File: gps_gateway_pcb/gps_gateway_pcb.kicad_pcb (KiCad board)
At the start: 2 copper layers, 53 x 32 mm, 72 parts, among them J1 Conn_01x06_Pin, J3 GNSS, J4 USB_OTG, J5 4G, J6 EG800, J7 SIM_Card, Q2 SS8050, Q3 SS8050, U1 Main, U2 TPS54202DDC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

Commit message: add ttl2rs485 module
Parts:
- added M1: RS485, UserLibrary:Module TTL to RS485 SMD, B.Cu at (98.3, 94.9)
- TP1: value RX -> TestPoint
- TP2: value TX -> TestPoint
- TP3: value RST -> TestPoint
- TP4: value BOOT -> TestPoint
- moved R24 1.22 mm to (93.2, 95.8)
- moved R25 1.22 mm to (93.2, 97.4)
- moved R26 1.22 mm to (93.2, 99.0)
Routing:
- net VCC33: track 77.2 -> 85.6 mm
- net /IO0: track 26.4 -> 27.5 mm
- net /IO1: track 28.5 -> 29.4 mm
- net /IO2: track 29.2 -> 28.4 mm
- net GND: vias 77 -> 80
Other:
- board text added: "BOOT"
- board text added: "RST"
- board text added: "RX"
- board text added: "TX"

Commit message: optimize pcb
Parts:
- removed D5: ST, LED_SMD:LED_0603_1608Metric
- TP1: value TestPoint -> IO5
- TP2: value TestPoint -> IO4
- TP3: value TestPoint -> RST
- TP4: value TestPoint -> BOOT
- moved TP2 11.7 mm to (88.1, 105.3)
- moved TP1 10.3 mm to (84.6, 104.4)
- moved R4 2.72 mm to (79.6, 109.0), turned to -90 degrees
- moved D4 1.91 mm to (91.5, 106.1)
- moved R9 1.12 mm to (91.5, 104.4), turned to 0 degrees
- moved R10 0.66 mm to (91.5, 102.8)
- moved R6 0.54 mm to (86.9, 106.8)
- moved R8 0.53 mm to (90.8, 100.0)
- moved R3 0.29 mm to (88.9, 106.8)
- moved R7 0.29 mm to (88.9, 103.7)
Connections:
- TP1 pad 1: /ESP_RX0 -> /IO5
- TP2 pad 1: /ESP_TX0 -> /IO4
- U3 pad 10: /ESP_TX_SIM -> /IO5
- U3 pad 27: /ESP_RX0 -> /ESP_RX_SIM
- U3 pad 28: /ESP_TX0 -> /ESP_TX_SIM
- U3 pad 9: /ESP_RX_SIM -> /IO4
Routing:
- net /ESP_TX_SIM: track 37.3 -> 28.1 mm
- net /ESP_RX_SIM: track 38.6 -> 31.7 mm
- net /IO4: track 0.00 -> 5.55 mm, vias 0 -> 1
- net /ESP_RX0: track 4.86 -> 0.00 mm, vias 1 -> 0
- net Net-(AE1-FEED): track 6.65 -> 4.13 mm
- net /IO5: track 0.00 -> 2.15 mm, vias 0 -> 1
- net GND: track 350.7 -> 348.7 mm, vias 80 -> 85
- net Net-(D6-A): track 5.18 -> 3.47 mm
- net /ESP_TX0: track 1.22 -> 0.00 mm, vias 1 -> 0
- net /Status: track 9.51 -> 8.86 mm
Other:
- board text added: "4G"
- board text added: "GPS"

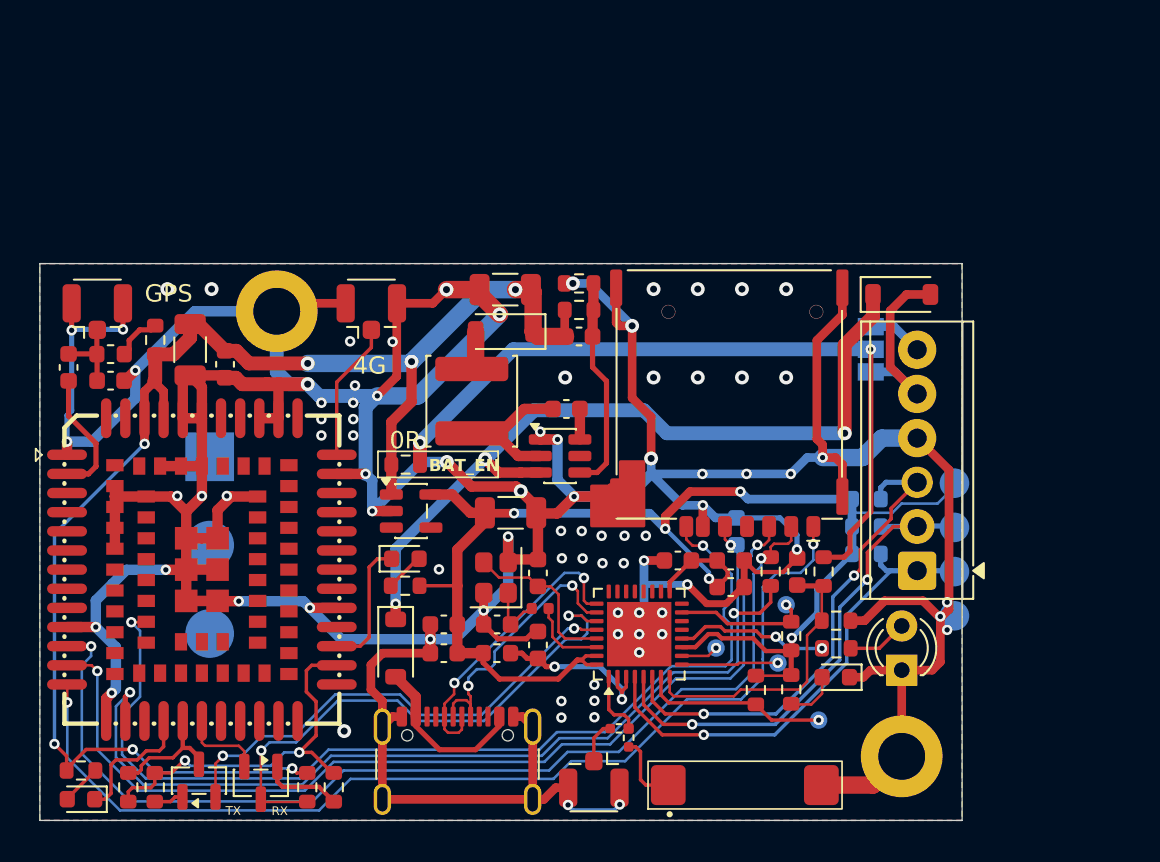
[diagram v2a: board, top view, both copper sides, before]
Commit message: change size
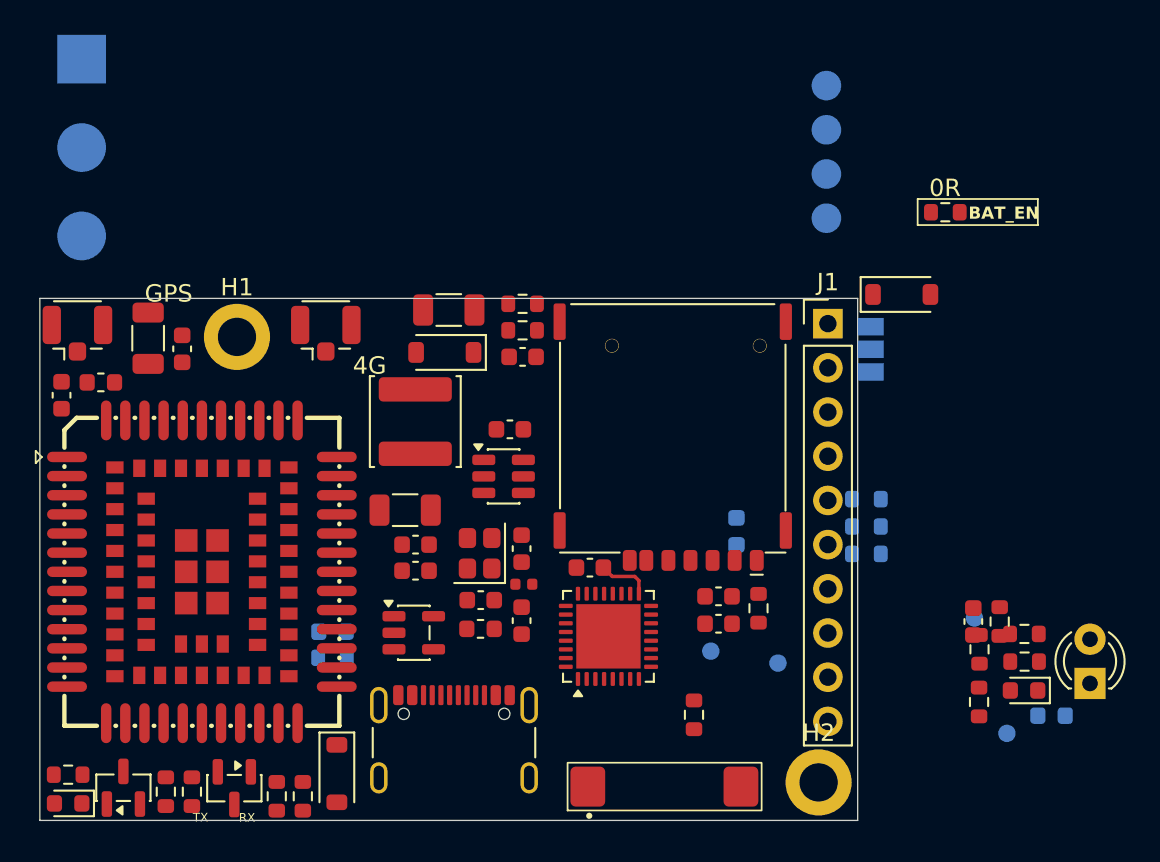
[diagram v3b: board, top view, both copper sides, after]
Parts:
- removed C19: 10uF, Capacitor_SMD:C_0603_1608Metric
- removed R11: 10, Resistor_SMD:R_0603_1608Metric
- removed R4: Res_3Pin, UserLibrary:Res3Pin 0402
- removed U1: Main, Connector_Coaxial:U.FL_Hirose_U.FL-R-SMT-1_Vertical
- added D5: ST, LED_SMD:LED_0603_1608Metric, B.Cu at (103.9, 108.3)
- D7, R12: moved to B.Cu
- H1, H2: footprint MountingHole:MountingHole_2.7mm_M2.5_DIN965_Pad -> MountingHole:MountingHole_2.2mm_M2_DIN965_Pad
- J1: value Conn_01x06_Pin -> Conn_01x10_Pin; footprint TerminalBlock_Phoenix:TerminalBlock_Phoenix_MPT-0,5-6-2.54_1x06_P2.54mm_Horizontal -> Connector_PinHeader_2.54mm:PinHeader_1x10_P2.54mm_Vertical
- moved R1 34.2 mm to (97.8, 79.3)
- moved M1 24.0 mm to (90.9, 72.1)
- moved J1 15.1 mm to (91.0, 85.8), turned to 0 degrees
- moved D4 10.8 mm to (102.3, 106.8)
- moved D6 10.8 mm to (106.1, 106.4)
- moved R9 10.8 mm to (102.3, 105.2)
- moved TP4 10.8 mm to (99.4, 102.7)
- moved R10 10.8 mm to (102.3, 103.6)
- moved R7 10.8 mm to (99.7, 104.5)
- moved TP3 10.8 mm to (101.3, 109.3)
- moved R3 10.8 mm to (99.7, 107.5)
- moved C14 10.5 mm to (99.4, 102.9)
- moved R8 10.5 mm to (100.9, 102.9)
- moved D1 7.97 mm to (62.8, 111.6)
- moved U4 7.00 mm to (67.2, 103.5)
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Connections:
- J1 pad 1: /IO0 -> Net-(J1-Pin_1)
- J1 pad 2: /IO1 -> Net-(D2-A)
- J1 pad 3: /IO2 -> GND
- J1 pad 4: GND -> /IO2
- J1 pad 5: Net-(D2-A) -> /IO1
- J1 pad 6: Net-(J1-Pin_6) -> /IO0
- J7 pad CD: /USIM_DET -> unconnected-(J7-PadCD)
- JP1 pad 3: Net-(J1-Pin_6) -> Net-(J1-Pin_1)
- L4 pad 2: Net-(L4-Pad2) -> SIM_VBAT
- U3 pad 1: Net-(R4-In) -> Net-(AE1-FEED)
- U3 pad 13: /MCU_IN1 -> /MCU_SIM_KEY
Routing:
- net GND: track 348.7 -> 0.00 mm, vias 85 -> 0
- net SIM_VBAT: track 83.6 -> 0.00 mm, vias 7 -> 0
- net VCC33: track 85.5 -> 3.10 mm, vias 5 -> 0
- net /USIM_DATA: track 60.6 -> 0.00 mm, vias 2 -> 0
- net /USIM_CLK: track 59.3 -> 0.00 mm, vias 2 -> 0
- net /USIM_DET: track 57.0 -> 0.00 mm, vias 2 -> 0
- net /USIM_VDD: track 56.6 -> 0.00 mm, vias 3 -> 0
- net /USIM_RST: track 56.3 -> 0.00 mm, vias 2 -> 0
- net Net-(D1-K): track 45.9 -> 0.00 mm, vias 3 -> 0
- net VOL_CHECK: track 42.6 -> 0.00 mm, vias 2 -> 0
- net /ESP_RX_SIM: track 31.7 -> 0.00 mm, vias 2 -> 0
- net /IO1: track 29.4 -> 0.00 mm, vias 2 -> 0
- net /IO2: track 28.4 -> 0.00 mm, vias 2 -> 0
- net /ESP_TX_SIM: track 28.1 -> 0.00 mm, vias 2 -> 0
- net /IO0: track 27.5 -> 0.00 mm, vias 1 -> 0
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- removed copper zone on B.Cu, net GND
- removed copper zone on F.Cu, net GND
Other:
- board size 53 x 32 mm -> 47 x 30 mm
